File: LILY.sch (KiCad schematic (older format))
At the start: 19 parts, among them U401 U-BLOX_LILY-W1, U402 AS179-92LF, X401 ANT

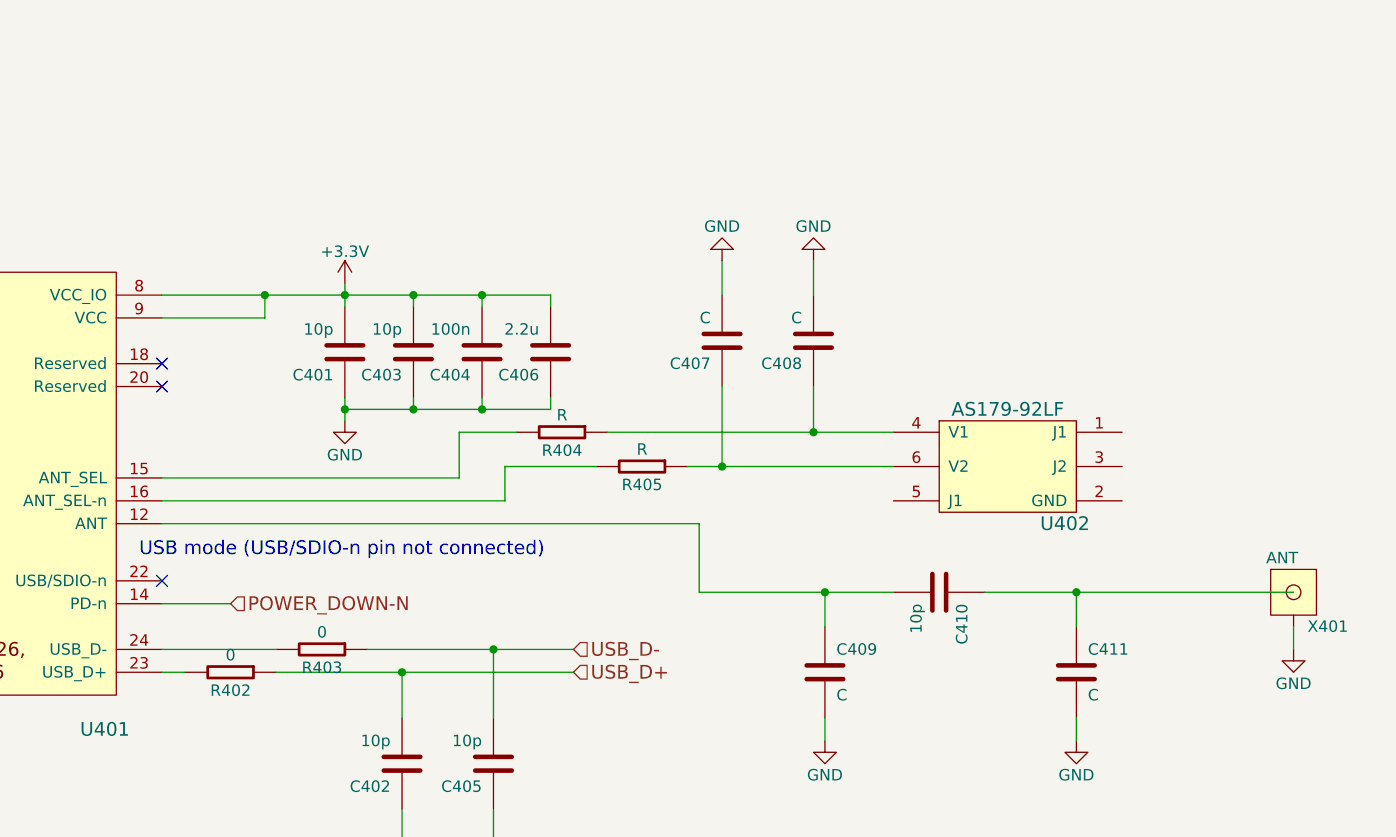
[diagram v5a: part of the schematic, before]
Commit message: adjusted power supply
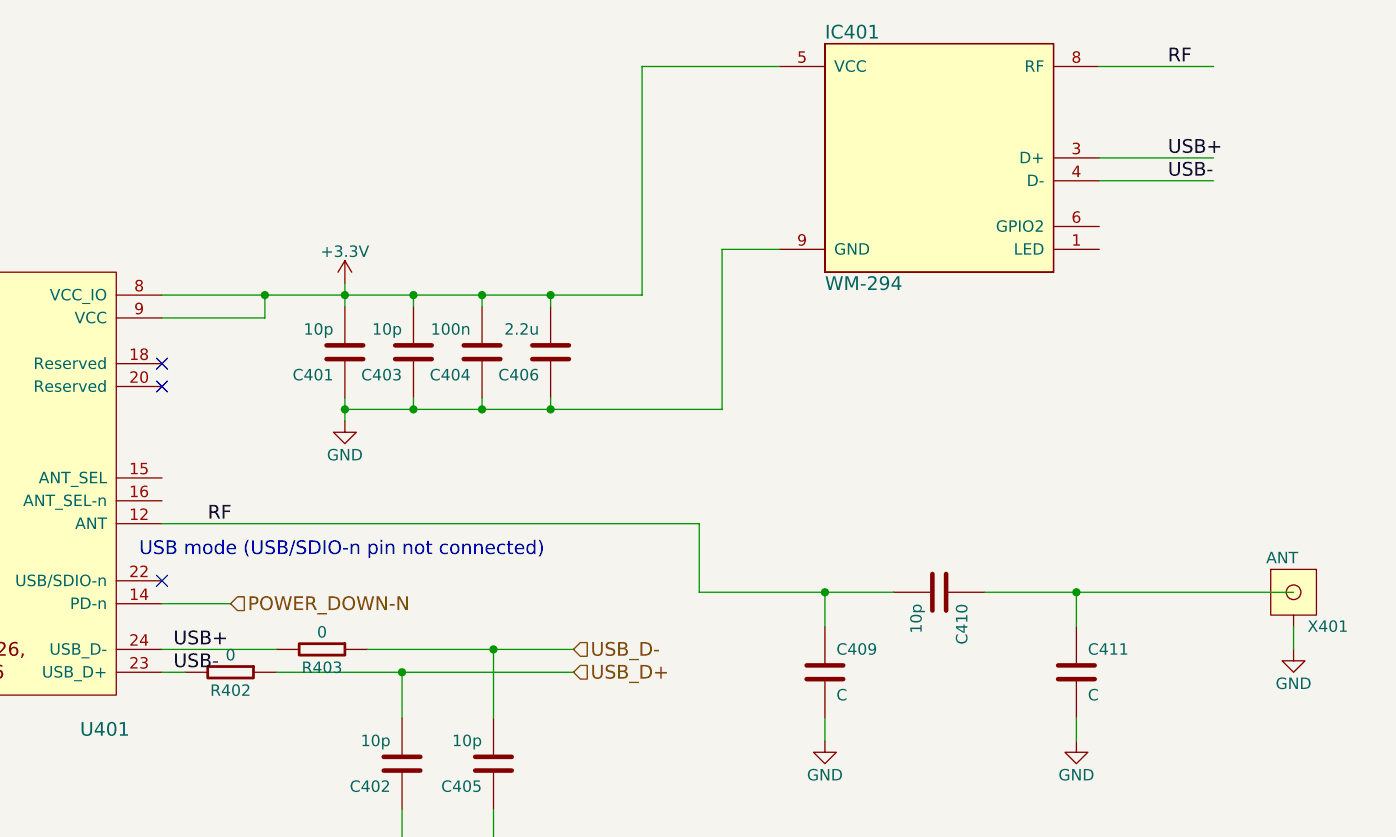
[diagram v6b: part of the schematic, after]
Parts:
- removed C407, C408: C, symbol C
- removed R404, R405: R, symbol R
- removed U402: AS179-92LF, symbol AS179-92LF
- added IC401: WM-294, Communication:WM-294, symbol WM-294
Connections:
- net labels added: RF, USB+, USB-
- wire segments 49 -> 44
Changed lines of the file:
@@
 NoConn ~ 2900 3550
 $Comp
-L GND #PWR0107
+L GND #PWR402
 U 1 1 57112756
 P 2600 4150
-F 0 "#PWR0107" H 2600 3900 50  0001 C CNN
+F 0 "#PWR402" H 2600 3900 50  0001 C CNN
 F 1 "GND" H 2600 4000 50  0000 C CNN
 F 2 "" H 2600 4150 50  0000 C CNN
@@
 Connection ~ 6350 4100
 $Comp
-L GND #PWR0108
+L GND #PWR406
 U 1 1 57112915
 P 6350 4950
-F 0 "#PWR0108" H 6350 4700 50  0001 C CNN
+F 0 "#PWR406" H 6350 4700 50  0001 C CNN
 F 1 "GND" H 6350 4800 50  0000 C CNN
 F 2 "" H 6350 4950 50  0000 C CNN
@@
 $EndComp
 $Comp
-L GND #PWR0109
+L GND #PWR405
 U 1 1 5711293E
 P 5950 4950
-F 0 "#PWR0109" H 5950 4700 50  0001 C CNN
+F 0 "#PWR405" H 5950 4700 50  0001 C CNN
 F 1 "GND" H 5950 4800 50  0000 C CNN
 F 2 "" H 5950 4950 50  0000 C CNN
@@
 Text HLabel 6700 4100 2    60   Input ~ 0
 USB_D-
-$Comp
-L AS179-92LF U402
-U 1 1 57112CC8
-P 8600 3300
-F 0 "U402" H 8850 3050 60  0000 C CNN
-F 1 "AS179-92LF" H 8600 3550 60  0000 C CNN
-F 2 "" H 8650 3300 60  0001 C CNN
-F 3 "" H 8650 3300 60  0000 C CNN
-	1    8600 3300
-	1    0    0    -1
-$EndComp
-$Comp
-L R R404
-U 1 1 57112D8E
-P 6650 3150
-F 0 "R404" V 6730 3150 50  0000 C CNN
-F 1 "R" V 6575 3150 50  0000 C CNN
-F 2 "" V 6580 3150 30  0001 C CNN
-F 3 "" H 6650 3150 30  0000 C CNN
-	1    6650 3150
-	0    1    1    0
-$EndComp
-$Comp
-L R R405
-U 1 1 57112DE1
-P 7000 3300
-F 0 "R405" V 7080 3300 50  0000 C CNN
-F 1 "R" V 6925 3300 50  0000 C CNN
-F 2 "" V 6930 3300 30  0001 C CNN
-F 3 "" H 7000 3300 30  0000 C CNN
-	1    7000 3300
-	0    1    1    0
-$EndComp
-Wire Wire Line
-	6850 3150 8100 3150
-Wire Wire Line
-	7200 3300 8100 3300
 Text HLabel 2650 2550 0    60   Input ~ 0
 WAKE_UP
@@
 POWER_DOWN-N
 $Comp
-L +3.3V #PWR0110
+L +3.3V #PWR403
 U 1 1 57149C0A
 P 5700 2500
-F 0 "#PWR0110" H 5700 2350 50  0001 C CNN
+F 0 "#PWR403" H 5700 2350 50  0001 C CNN
 F 1 "+3.3V" H 5700 2640 50  0000 C CNN
 F 2 "" H 5700 2500 50  0000 C CNN
@@
 	4900 3900 5200 3900
 $Comp
-L GND #PWR0111
+L GND #PWR404
 U 1 1 5714A025
 P 5700 3100
-F 0 "#PWR0111" H 5700 2850 50  0001 C CNN
+F 0 "#PWR404" H 5700 2850 50  0001 C CNN
 F 1 "GND" H 5700 2950 50  0000 C CNN
 F 2 "" H 5700 3100 50  0000 C CNN
@@
 $EndComp
 Wire Wire Line
-	4900 2550 6600 2550
+	4900 2550 7000 2550
 Wire Wire Line
 	5350 2650 4900 2650
@@
 	5000 4200 4900 4200
 Wire Wire Line
-	4900 3350 6200 3350
-Wire Wire Line
-	6200 3350 6200 3150
-Wire Wire Line
-	4900 3450 6400 3450
-Wire Wire Line
-	6400 3450 6400 3300
-Wire Wire Line
 	5700 2500 5700 2600
 Connection ~ 5700 2550
@@
 Wire Wire Line
 	5700 3000 5700 3100
-Wire Wire Line
-	6200 3150 6450 3150
-Wire Wire Line
-	6400 3300 6800 3300
-$Comp
-L C C408
-U 1 1 572263E0
-P 7750 2750
-F 0 "C408" H 7800 2850 50  0000 L CNN
-F 1 "C" H 7800 2650 50  0000 L CNN
-F 2 "" H 7788 2600 30  0001 C CNN
-F 3 "" H 7800 2850 60  0000 C CNN
-	1    7750 2750
-	-1   0    0    1
-$EndComp
-$Comp
-L C C407
-U 1 1 572263E6
-P 7350 2750
-F 0 "C407" H 7400 2850 50  0000 L CNN
-F 1 "C" H 7400 2650 50  0000 L CNN
-F 2 "" H 7388 2600 30  0001 C CNN
-F 3 "" H 7400 2850 60  0000 C CNN
-	1    7350 2750
-	-1   0    0    1
-$EndComp
-Wire Wire Line
-	7750 3150 7750 2950
-Wire Wire Line
-	7350 3300 7350 2950
-$Comp
-L GND #PWR0112
-U 1 1 572263EE
-P 7350 2400
-F 0 "#PWR0112" H 7350 2150 50  0001 C CNN
-F 1 "GND" H 7350 2250 50  0000 C CNN
-F 2 "" H 7350 2400 50  0000 C CNN
-F 3 "" H 7350 2400 50  0000 C CNN
-	1    7350 2400
-	-1   0    0    1
-$EndComp
-$Comp
-L GND #PWR0113
-U 1 1 572263F4
-P 7750 2400
-F 0 "#PWR0113" H 7750 2150 50  0001 C CNN
-F 1 "GND" H 7750 2250 50  0000 C CNN
-F 2 "" H 7750 2400 50  0000 C CNN
-F 3 "" H 7750 2400 50  0000 C CNN
-	1    7750 2400
-	-1   0    0    1
-$EndComp
-Wire Wire Line
-	7350 2400 7350 2550
-Wire Wire Line
-	7750 2550 7750 2400
-Connection ~ 7750 3150
-Connection ~ 7350 3300
 $Comp
 L C C409
@@
 $EndComp
 $Comp
-L GND #PWR0114
+L GND #PWR407
 U 1 1 57226BCE
 P 7800 4500
-F 0 "#PWR0114" H 7800 4250 50  0001 C CNN
+F 0 "#PWR407" H 7800 4250 50  0001 C CNN
 F 1 "GND" H 7800 4350 50  0000 C CNN
 F 2 "" H 7800 4500 50  0000 C CNN
@@
 $EndComp
 $Comp
-L GND #PWR0115
+L GND #PWR408
 U 1 1 57226C0F
 P 8900 4500
-F 0 "#PWR0115" H 8900 4250 50  0001 C CNN
+F 0 "#PWR408" H 8900 4250 50  0001 C CNN
 F 1 "GND" H 8900 4350 50  0000 C CNN
 F 2 "" H 8900 4500 50  0000 C CNN
@@
 	7800 4400 7800 4500
 $Comp
-L GND #PWR0116
+L GND #PWR409
 U 1 1 57226CCB
 P 9850 4100
-F 0 "#PWR0116" H 9850 3850 50  0001 C CNN
+F 0 "#PWR409" H 9850 3850 50  0001 C CNN
 F 1 "GND" H 9850 3950 50  0000 C CNN
 F 2 "" H 9850 4100 50  0000 C CNN
@@
 $EndComp
 $Comp
-L +3.3V #PWR0117
+L +3.3V #PWR401
 U 1 1 572270BD
 P 1700 3600
-F 0 "#PWR0117" H 1700 3450 50  0001 C CNN
+F 0 "#PWR401" H 1700 3450 50  0001 C CNN
 F 1 "+3.3V" H 1700 3740 50  0000 C CNN
 F 2 "" H 1700 3600 50  0000 C CNN
@@
 	6000 3000 6000 3050
 Wire Wire Line
-	5700 3050 6600 3050
+	5700 3050 7350 3050
 Connection ~ 5700 3050
 Wire Wire Line
@@
 	-1   0    0    1
 $EndComp
+$Comp
+L WM-294 IC401
+U 1 1 5728BEA1
+P 8300 1950
+F 0 "IC401" H 7800 2500 60  0000 L CNN
+F 1 "WM-294" H 7800 1400 60  0000 L CNN
+F 2 "Communication:WM-294" H 7400 -6325 60  0001 C CNN
+F 3 "" H 7400 -6325 60  0000 C CNN
+	1    8300 1950
+	1    0    0    -1
+$EndComp
+Wire Wire Line
+	7000 2550 7000 1550
+Wire Wire Line
+	7000 1550 7600 1550
+Connection ~ 6600 2550
+Wire Wire Line
+	7350 3050 7350 2350
+Wire Wire Line
+	7350 2350 7600 2350
+Connection ~ 6600 3050
+Text Label 4950 4100 0    60   ~ 0
+USB+
+Text Label 4950 4200 0    60   ~ 0
+USB-
+Wire Wire Line
+	9500 1950 9000 1950
+Wire Wire Line
+	9000 2050 9500 2050
+Text Label 9300 1950 0    60   ~ 0
+USB+
+Text Label 9300 2050 0    60   ~ 0
+USB-
+Wire Wire Line
+	9000 1550 9500 1550
+Text Label 9300 1550 0    60   ~ 0
+RF
+Text Label 5100 3550 0    60   ~ 0
+RF
 $EndSCHEMATC

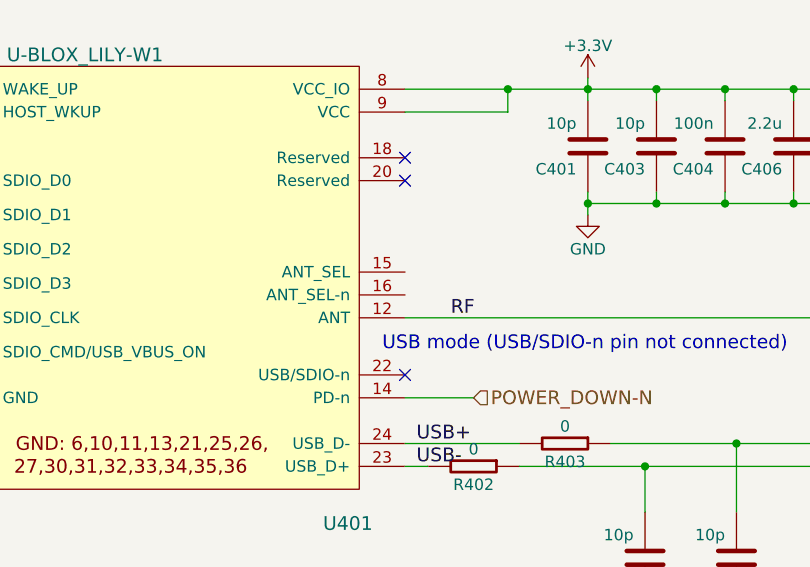
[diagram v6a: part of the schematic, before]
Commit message: adjusted power supply and sensors
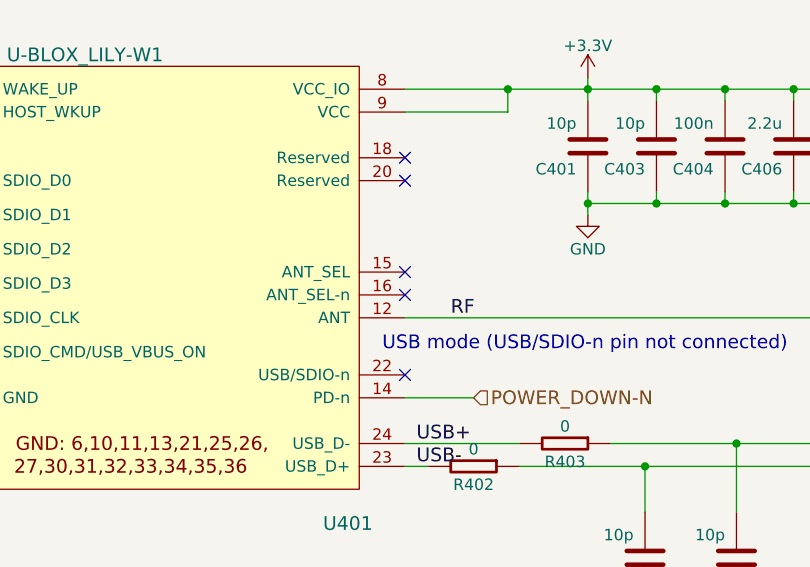
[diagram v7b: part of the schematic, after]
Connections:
- no-connect marks 8 -> 10
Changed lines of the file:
@@
 Text Label 5100 3550 0    60   ~ 0
 RF
+NoConn ~ 4900 3350
+NoConn ~ 4900 3450
 $EndSCHEMATC

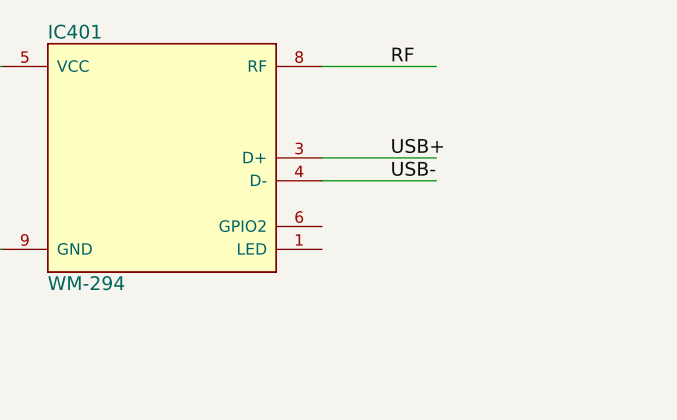
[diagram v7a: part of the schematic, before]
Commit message: adjusted 3d models
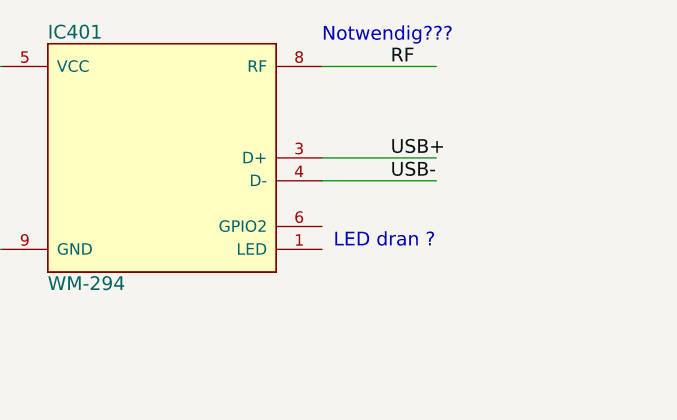
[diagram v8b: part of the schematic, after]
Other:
- note added: "LED dran ?"
- note added: "Notwendig???\n"
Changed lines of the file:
@@
 NoConn ~ 2900 3550
 $Comp
-L GND #PWR402
+L GND #PWR0107
 U 1 1 57112756
 P 2600 4150
-F 0 "#PWR402" H 2600 3900 50  0001 C CNN
+F 0 "#PWR0107" H 2600 3900 50  0001 C CNN
 F 1 "GND" H 2600 4000 50  0000 C CNN
 F 2 "" H 2600 4150 50  0000 C CNN
@@
 Connection ~ 6350 4100
 $Comp
-L GND #PWR406
+L GND #PWR0108
 U 1 1 57112915
 P 6350 4950
-F 0 "#PWR406" H 6350 4700 50  0001 C CNN
+F 0 "#PWR0108" H 6350 4700 50  0001 C CNN
 F 1 "GND" H 6350 4800 50  0000 C CNN
 F 2 "" H 6350 4950 50  0000 C CNN
@@
 $EndComp
 $Comp
-L GND #PWR405
+L GND #PWR0109
 U 1 1 5711293E
 P 5950 4950
-F 0 "#PWR405" H 5950 4700 50  0001 C CNN
+F 0 "#PWR0109" H 5950 4700 50  0001 C CNN
 F 1 "GND" H 5950 4800 50  0000 C CNN
 F 2 "" H 5950 4950 50  0000 C CNN
@@
 POWER_DOWN-N
 $Comp
-L +3.3V #PWR403
+L +3.3V #PWR0110
 U 1 1 57149C0A
 P 5700 2500
-F 0 "#PWR403" H 5700 2350 50  0001 C CNN
+F 0 "#PWR0110" H 5700 2350 50  0001 C CNN
 F 1 "+3.3V" H 5700 2640 50  0000 C CNN
 F 2 "" H 5700 2500 50  0000 C CNN
@@
 	4900 3900 5200 3900
 $Comp
-L GND #PWR404
+L GND #PWR0111
 U 1 1 5714A025
 P 5700 3100
-F 0 "#PWR404" H 5700 2850 50  0001 C CNN
+F 0 "#PWR0111" H 5700 2850 50  0001 C CNN
 F 1 "GND" H 5700 2950 50  0000 C CNN
 F 2 "" H 5700 3100 50  0000 C CNN
@@
 $EndComp
 $Comp
-L GND #PWR407
+L GND #PWR0112
 U 1 1 57226BCE
 P 7800 4500
-F 0 "#PWR407" H 7800 4250 50  0001 C CNN
+F 0 "#PWR0112" H 7800 4250 50  0001 C CNN
 F 1 "GND" H 7800 4350 50  0000 C CNN
 F 2 "" H 7800 4500 50  0000 C CNN
@@
 $EndComp
 $Comp
-L GND #PWR408
+L GND #PWR0113
 U 1 1 57226C0F
 P 8900 4500
-F 0 "#PWR408" H 8900 4250 50  0001 C CNN
+F 0 "#PWR0113" H 8900 4250 50  0001 C CNN
 F 1 "GND" H 8900 4350 50  0000 C CNN
 F 2 "" H 8900 4500 50  0000 C CNN
@@
 	7800 4400 7800 4500
 $Comp
-L GND #PWR409
+L GND #PWR0114
 U 1 1 57226CCB
 P 9850 4100
-F 0 "#PWR409" H 9850 3850 50  0001 C CNN
+F 0 "#PWR0114" H 9850 3850 50  0001 C CNN
 F 1 "GND" H 9850 3950 50  0000 C CNN
 F 2 "" H 9850 4100 50  0000 C CNN
@@
 $EndComp
 $Comp
-L +3.3V #PWR401
+L +3.3V #PWR0115
 U 1 1 572270BD
 P 1700 3600
-F 0 "#PWR401" H 1700 3450 50  0001 C CNN
+F 0 "#PWR0115" H 1700 3450 50  0001 C CNN
 F 1 "+3.3V" H 1700 3740 50  0000 C CNN
 F 2 "" H 1700 3600 50  0000 C CNN
@@
 NoConn ~ 4900 3350
 NoConn ~ 4900 3450
+Text Notes 9000 1450 0    60   ~ 0
+Notwendig???\n
+Text Notes 9050 2350 0    60   ~ 0
+LED dran ?
 $EndSCHEMATC
